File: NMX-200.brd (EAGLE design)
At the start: 67.3 x 63.5 mm, 93 parts, among them IC1 AT90USB1287-AU, IC2 AT90USB1287-MU, J1 PJ-002AH, J2 10118193-0001LF, J3 SJ1-2503A, J4 RJHSE-5385-02, J5 SJ1-2503A, J6 SJ1-2503A, Q1 P-CHANNEL_MOSFET, T1 CMPT2369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

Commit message: Fixed NMX-200 schematic typo
Two 10k resistors were marked with an upper case "K" instead of lower
case k", which caused them to appear as a separate line on the exported
BOM.
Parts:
- R4, R5: value 10K -> 10k
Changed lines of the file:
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@@
 <?xml version="1.0" encoding="utf-8"?>
 <!DOCTYPE eagle SYSTEM "eagle.dtd">
-<eagle version="6.6.0">
+<eagle version="6.5.0">
 <drawing>
 <settings>
@@
 <attribute name="NAME" x="12.16875" y="19.51875" size="0.8128" layer="25" font="vector" rot="R90"/>
 </element>
-<element name="R4" library="resistor" package="R0402" value="10K" x="6.35" y="19.05" smashed="yes" rot="MR90">
+<element name="R4" library="resistor" package="R0402" value="10k" x="6.35" y="19.05" smashed="yes" rot="MR90">
 <attribute name="MPN" value="RC0402FR-0710KL" x="-77.47" y="90.17" size="1.778" layer="28" rot="MR90" display="off"/>
 <attribute name="MF" value="Yageo" x="-77.47" y="90.17" size="1.778" layer="28" rot="MR90" display="off"/>
@@
 <attribute name="VALUE" x="11.8745" y="46.355" size="0.8128" layer="27" rot="R90"/>
 </element>
-<element name="R5" library="resistor" package="R0402" value="10K" x="11.43" y="39.37" smashed="yes" rot="MR180">
+<element name="R5" library="resistor" package="R0402" value="10k" x="11.43" y="39.37" smashed="yes" rot="MR180">
 <attribute name="MPN" value="RC0402FR-0710KL" x="86.36" y="123.19" size="1.778" layer="28" rot="MR180" display="off"/>
 <attribute name="MF" value="Yageo" x="86.36" y="123.19" size="1.778" layer="28" rot="MR180" display="off"/>

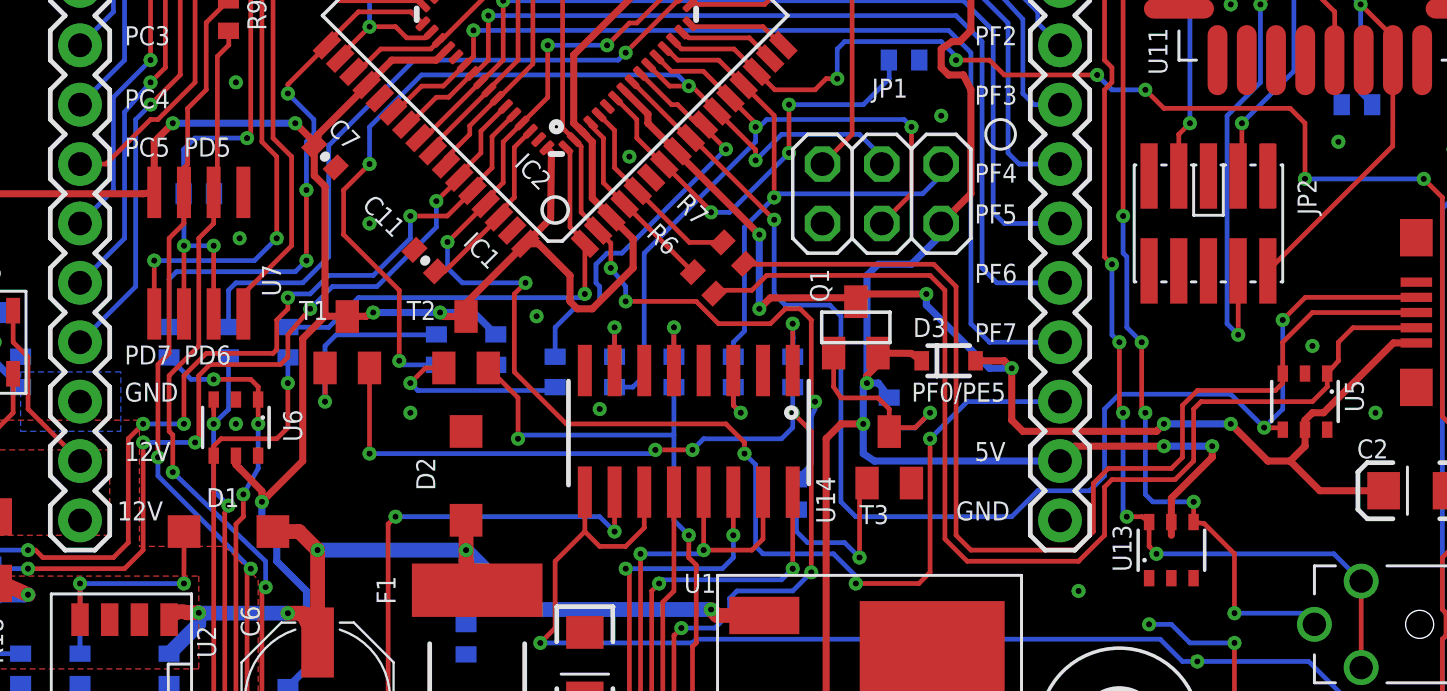
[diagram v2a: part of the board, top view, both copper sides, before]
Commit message: Changed silkscreen to indicate polarity of some components
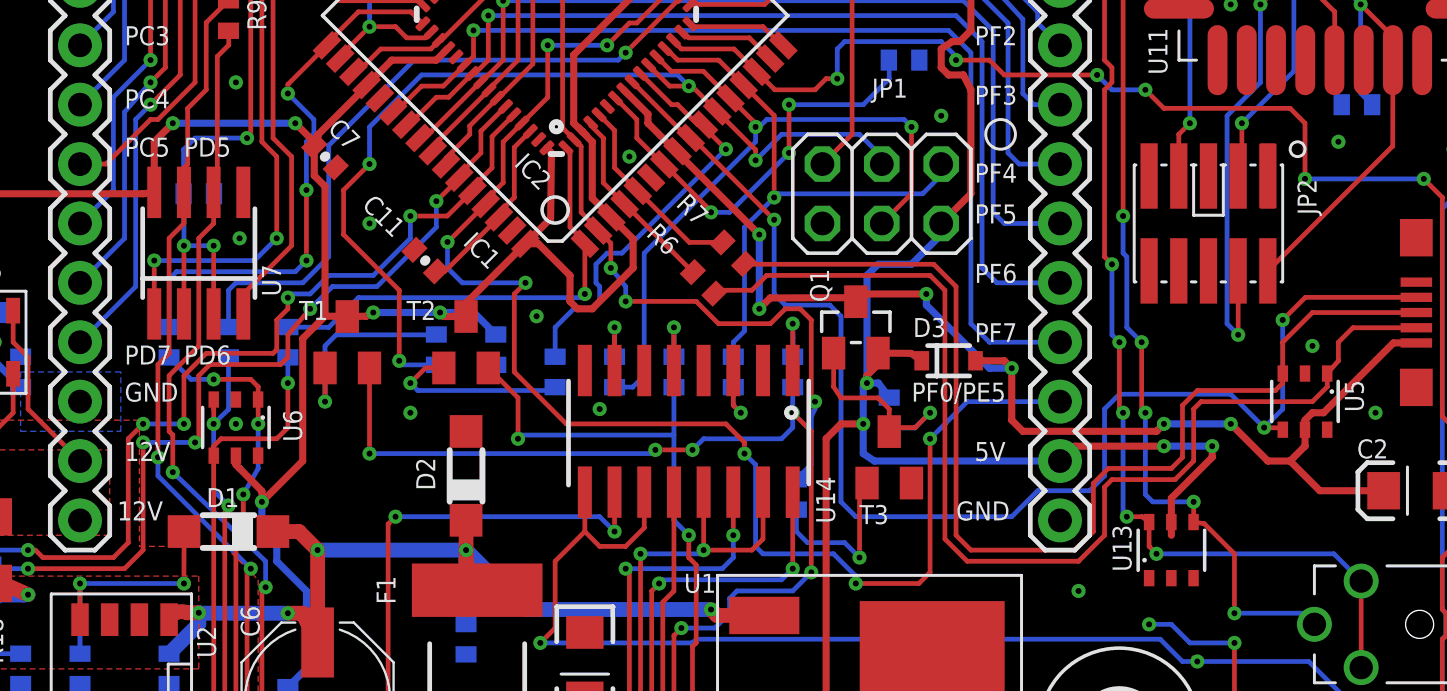
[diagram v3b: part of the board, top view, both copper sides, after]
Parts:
- D2: device NMX_ControllerSide_v1-3:SOD123 -> diode:SOD123
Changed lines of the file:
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@@
 <?xml version="1.0" encoding="utf-8"?>
 <!DOCTYPE eagle SYSTEM "eagle.dtd">
-<eagle version="6.5.0">
+<eagle version="6.6.0">
 <drawing>
 <settings>
@@
 <attribute name="VALUE" x="35.30346875" y="35.346659375" size="0.8128" layer="27" rot="R315"/>
 </element>
-<element name="D2" library="NMX_ControllerSide_v1-3" package="SOD123" value="MMSZ5253B" x="22.86" y="27.305" smashed="yes" rot="R90">
+<element name="D2" library="diode" package="SOD123" value="MMSZ5253B" x="22.86" y="27.305" smashed="yes" rot="R90">
 <attribute name="MPN" value="MMSZ5253B" x="101.6" y="70.485" size="1.778" layer="27" rot="R90" display="off"/>
 <attribute name="MF" value="Fairchild Semiconductor" x="101.6" y="70.485" size="1.778" layer="27" rot="R90" display="off"/>
